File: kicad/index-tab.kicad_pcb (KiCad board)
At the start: 2 copper layers, 254 x 140.1 mm, 179 parts, among them J1 USB_C_Receptacle_USB2.0, SW1 SW_Push, U1 ATmega32U4-MU, U2 MIC5219-5.0YM5, Y1 16MHz

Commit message: Switched to 0603 and redrawn the PCB
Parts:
- removed C9: 100nF, Capacitor_SMD:C_1206_3216Metric_Pad1.42x1.75mm_HandSolder
- removed D101: PRTR5V0U2X, Package_TO_SOT_SMD:SOT-143
- removed D103: LED, LED_SMD:LED_1206_3216Metric_Pad1.42x1.75mm_HandSolder
- removed REF** (x2): Stabilizer_MX_2u, index-tab:Stabilizer_MX_2u
- removed U2: MIC5219-5.0YM5, Package_TO_SOT_SMD:SOT-23-5_HandSoldering
- added LED1: LED, LED_SMD:LED_0603_1608Metric_Pad1.05x0.95mm_HandSolder, B.Cu at (275.9, 44.8)
- C1, C2, C4: footprint Capacitor_SMD:C_1206_3216Metric_Pad1.42x1.75mm_HandSolder -> Capacitor_SMD:C_0603_1608Metric_Pad1.05x0.95mm_HandSolder
- C3: value 100nF -> 0.1uF; footprint Capacitor_SMD:C_1206_3216Metric_Pad1.42x1.75mm_HandSolder -> Capacitor_SMD:C_0603_1608Metric_Pad1.05x0.95mm_HandSolder
- C5: value 1uF -> 10uF; footprint Capacitor_SMD:C_1206_3216Metric_Pad1.42x1.75mm_HandSolder -> Capacitor_SMD:C_0603_1608Metric_Pad1.05x0.95mm_HandSolder
- C6, C7: value 10uF -> 1uF; footprint Capacitor_SMD:C_1206_3216Metric_Pad1.42x1.75mm_HandSolder -> Capacitor_SMD:C_0603_1608Metric_Pad1.05x0.95mm_HandSolder
- C8: value 1uF -> 0.1uF; footprint Capacitor_SMD:C_1206_3216Metric_Pad1.42x1.75mm_HandSolder -> Capacitor_SMD:C_0603_1608Metric_Pad1.05x0.95mm_HandSolder
- D1, D10, D11, D12, D13, D14, D15, D16, D17, D18, D19, D2, D20, D21, D22, D23, D24, D25, D26, D27, D28, D29, D3, D30, D31, D32, D33, D34, D35, D36, D37, D38, D39, D4, D40, D41, D42, D43, D44, D45, D46, D47, D48, D49, D5, D50, D51, D52, D53, D54, D55, D56, D57, D58, D59, D6, D60, D61, D62, D63, D64, D65, D66, D67, D68, D69, D7, D70, D71, D72, D73, D74, D75, D76, D8, D9: footprint Diode_SMD:D_1206_3216Metric_Pad1.42x1.75mm_HandSolder -> Diode_SMD:D_0603_1608Metric_Pad1.05x0.95mm_HandSolder
- D102: value D -> 3A/10V/280mV; footprint Diode_SMD:D_1206_3216Metric_Pad1.42x1.75mm_HandSolder -> Diode_SMD:D_SOD-323_HandSoldering
- F1: value 500mA -> 6v 0.5A
- R1, R2, R3, R4, R5, R6, R7: footprint Resistor_SMD:R_1206_3216Metric_Pad1.42x1.75mm_HandSolder -> Resistor_SMD:R_0603_1608Metric_Pad1.05x0.95mm_HandSolder
- U1: value ATmega32U4-MU -> ATmega32U4-AU; footprint Package_DFN_QFN:QFN-44-1EP_7x7mm_P0.5mm_EP5.2x5.2mm -> Package_QFP:TQFP-44_10x10mm_P0.8mm
- Y1: footprint Crystal:Crystal_SMD_3225-4Pin_3.2x2.5mm_HandSoldering -> Crystal:Crystal_SMD_0603-4Pin_6.0x3.5mm
- moved C7 53.6 mm to (270.6, 43.2)
- moved F1 42.8 mm to (268.0, 36.5), turned to 0 degrees
- moved D102 42.1 mm to (263.2, 36.5), turned to 0 degrees
- moved C6 40.4 mm to (254.9, 30.6), turned to 45 degrees
- moved C8 37.1 mm to (230.9, 34.0), turned to 180 degrees
- moved R5 33.1 mm to (257.3, 36.8), turned to 0 degrees
- moved C4 31.3 mm to (259.4, 30.8), turned to 0 degrees
- moved C2 17.9 mm to (256.9, 42.9), turned to 45 degrees
- moved C3 16.8 mm to (234.3, 27.0)
- moved C1 16.7 mm to (259.4, 40.4), turned to 45 degrees
- moved Y1 15.4 mm to (263.9, 44.0), turned to 180 degrees
- moved R4 13.4 mm to (251.4, 27.4), turned to 45 degrees
- moved C5 13.0 mm to (230.9, 31.0), turned to 180 degrees
- moved U1 9.24 mm to (245.6, 36.4), turned to 225 degrees
- moved R6 8.67 mm to (234.1, 38.2), turned to 0 degrees
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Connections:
- net Net-(C4-Pad1) renamed /UCAP
- net Net-(R5-Pad1) renamed /RESET
- C3 pad 1: GND -> /AREF
- C3 pad 2: Net-(C3-Pad2) -> GND
- C5 pad 1: /UVCC -> /+5v
- C6 pad 1: Net-(C6-Pad1) -> /V_USB
- C7 pad 1: /VCC -> /+5v
- C8 pad 1: /VCC -> /+5v
- D102 pad 1: Net-(C6-Pad1) -> /+5v
- F1 pad 1: /UVCC -> Net-(D102-Pad2)
- F1 pad 2: Net-(D102-Pad2) -> /V_USB
- J1 pad A4: /UVCC -> /V_USB
- J1 pad A6: Net-(D101-Pad2) -> /D+
- J1 pad A7: Net-(D101-Pad3) -> /D-
- J1 pad A9: /UVCC -> /V_USB
- J1 pad B4: /UVCC -> /V_USB
- J1 pad B6: Net-(D101-Pad2) -> /D+
- J1 pad B7: Net-(D101-Pad3) -> /D-
- J1 pad B9: /UVCC -> /V_USB
- J1 pad S1: GND -> Net-(J1-PadS1)
- R1 pad 1: Net-(J1-PadA5) -> GND
- R1 pad 2: GND -> Net-(J1-PadA5)
- R3 pad 2: Net-(D101-Pad3) -> /D+
- R4 pad 2: Net-(D101-Pad2) -> /D-
- R5 pad 2: /VCC -> /+5v
- R7 pad 1: /VCC -> Net-(LED1-Pad2)
- R7 pad 2: Net-(D103-Pad2) -> /+5v
- U1 pad 10: COL7 -> Net-(U1-Pad10)
- U1 pad 11: COL6 -> Net-(U1-Pad11)
- U1 pad 12: COL5 -> Net-(U1-Pad12)
- U1 pad 14: /VCC -> /+5v
- U1 pad 18: COL4 -> ROW5
- U1 pad 19: COL3 -> ROW4
- U1 pad 2: /UVCC -> /V_USB
- U1 pad 20: COL2 -> ROW3
- U1 pad 21: COL1 -> ROW2
- U1 pad 22: COL0 -> ROW1
- U1 pad 24: /VCC -> /+5v
- U1 pad 25: Net-(U1-Pad25) -> ROW0
- U1 pad 26: Net-(U1-Pad26) -> COL12
- U1 pad 27: ROW5 -> COL11
- U1 pad 28: ROW4 -> COL10
- U1 pad 29: ROW3 -> COL9
- U1 pad 3: Net-(R3-Pad1) -> Net-(R4-Pad1)
- U1 pad 30: ROW2 -> COL8
- U1 pad 31: ROW1 -> COL7
- U1 pad 32: ROW0 -> COL6
- U1 pad 34: /VCC -> /+5v
- U1 pad 36: Net-(U1-Pad36) -> COL5
- U1 pad 37: Net-(U1-Pad37) -> COL4
- U1 pad 38: Net-(U1-Pad38) -> COL3
- U1 pad 39: COL12 -> COL2
- U1 pad 4: Net-(R4-Pad1) -> Net-(R3-Pad1)
- U1 pad 40: COL11 -> COL1
- U1 pad 41: COL10 -> COL0
- U1 pad 42: Net-(C3-Pad2) -> /AREF
- U1 pad 44: /VCC -> /+5v
- U1 pad 7: /UVCC -> /V_USB
- U1 pad 8: COL9 -> Net-(U1-Pad8)
- U1 pad 9: COL8 -> Net-(U1-Pad9)
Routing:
- net /VCC: track 177.5 -> 0.00 mm, vias 3 -> 0
- net /UVCC: track 121.3 -> 0.00 mm, vias 2 -> 0
- net /+5v: track 0.00 -> 74.0 mm, vias 0 -> 2
- net GND: track 267.3 -> 198.5 mm
- net ROW0: track 300.9 -> 253.3 mm
- net /V_USB: track 0.00 -> 40.8 mm
- net /D-: track 0.00 -> 31.2 mm, vias 0 -> 2
- net /D+: track 0.00 -> 28.9 mm, vias 0 -> 2
- net Net-(R3-Pad1): track 32.5 -> 4.68 mm, vias 2 -> 0
- net Net-(D101-Pad3): track 27.6 -> 0.00 mm, vias 2 -> 0
- net Net-(R4-Pad1): track 30.5 -> 3.93 mm, vias 2 -> 0
- net /RESET: track 15.9 -> 41.9 mm, vias 0 -> 2
- net Net-(D101-Pad2): track 25.5 -> 0.00 mm
- net Net-(C6-Pad1): track 18.9 -> 0.00 mm
- net /XTAL1: track 32.0 -> 13.1 mm
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- removed copper zone on B.Cu, net GND

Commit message: Added rounded corners to the pcb
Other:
- board size 254 x 140.1 mm -> 254 x 140 mm
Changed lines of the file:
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@@
   (general
     (thickness 1.6)
-    (drawings 7)
+    (drawings 14)
     (tracks 1074)
     (zones 0)
@@
       (net 88 COL0))
   )
-  (gr_line (start 210.75 36) (end 210.75 44) (layer Edge.Cuts) (width 0.12))
-  (gr_line (start 210.75 36) (end 221.85 24.95) (layer Edge.Cuts) (width 0.12))
-  (gr_line (start 279 24.95) (end 221.85 24.95) (layer Edge.Cuts) (width 0.12))
-  (gr_line (start 25 44) (end 25 165) (layer Edge.Cuts) (width 0.12))
-  (gr_line (start 279 165) (end 279 24.95) (layer Edge.Cuts) (width 0.12))
-  (gr_line (start 25 165) (end 279 165) (layer Edge.Cuts) (width 0.12))
-  (gr_line (start 25 44) (end 210.75 44) (layer Edge.Cuts) (width 0.12))
+  (gr_arc (start 211.15 36) (end 210.9 35.7) (angle -50.21937124) (layer Edge.Cuts) (width 0.12))
+  (gr_arc (start 222 25.5) (end 222 25) (angle -48.81407483) (layer Edge.Cuts) (width 0.12))
+  (gr_arc (start 278.5 164.5) (end 278.5 165) (angle -90) (layer Edge.Cuts) (width 0.12))
+  (gr_arc (start 25.5 164.5) (end 25 164.5) (angle -90) (layer Edge.Cuts) (width 0.12))
+  (gr_arc (start 25.5 44.5) (end 25.5 44) (angle -90) (layer Edge.Cuts) (width 0.12))
+  (gr_arc (start 210.25 43.5) (end 210.25 44) (angle -90) (layer Edge.Cuts) (width 0.12))
+  (gr_arc (start 278 26) (end 279 26) (angle -90) (layer Edge.Cuts) (width 0.12))
+  (gr_line (start 210.759488 36.00017) (end 210.75 43.5) (layer Edge.Cuts) (width 0.12))
+  (gr_line (start 210.9 35.7) (end 221.623712 25.170748) (layer Edge.Cuts) (width 0.12))
+  (gr_line (start 278 25) (end 222 25) (layer Edge.Cuts) (width 0.12))
+  (gr_line (start 25 44.5) (end 25 164.5) (layer Edge.Cuts) (width 0.12))
+  (gr_line (start 279 164.5) (end 279 26) (layer Edge.Cuts) (width 0.12))
+  (gr_line (start 25.5 165) (end 278.5 165) (layer Edge.Cuts) (width 0.12))
+  (gr_line (start 25.5 44) (end 210.25 44) (layer Edge.Cuts) (width 0.12))
   (segment (start 264.112564 39.762564) (end 260.592685 39.762564) (width 0.25) (layer B.Cu) (net 1))
   (segment (start 260.592685 39.762564) (end 259.987436 39.762564) (width 0.25) (layer B.Cu) (net 1))

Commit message: Moved some components for better fillzone
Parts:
- moved C8 29.2 mm to (260.0, 35.6), turned to 90 degrees
- moved C5 26.6 mm to (257.3, 34.7)
- moved C7 12.9 mm to (261.9, 33.7), turned to 90 degrees
- moved C6 10.4 mm to (265.2, 30.1), turned to 0 degrees
- moved C4 6.42 mm to (265.2, 28.1)
- moved R4 2.57 mm to (253.9, 27.7), turned to 0 degrees
- moved R3 1.45 mm to (253.9, 29.4), turned to 0 degrees
- moved R1 0.81 mm to (275.7, 27.8)
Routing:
- net GND: track 198.5 -> 12.2 mm, vias 0 -> 13
- net /+5v: track 74.0 -> 80.4 mm, vias 2 -> 4
- net /UCAP: track 10.0 -> 16.5 mm
- net /D-: track 31.2 -> 27.2 mm
- net /D+: track 28.9 -> 25.6 mm
- net Net-(R4-Pad1): track 3.93 -> 6.32 mm
- net Net-(R3-Pad1): track 4.68 -> 6.31 mm
- net (no net): track 0.00 -> 1.51 mm
- net /V_USB: track 40.8 -> 39.6 mm
- net Net-(J1-PadA5): track 7.89 -> 7.05 mm
- added copper zone on B.Cu, net GND
- added copper zone on F.Cu, net GND
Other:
- net class Power added: clearance 0.2, trace_width 0.381, via_dia 0.8, via_drill 0.4

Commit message: Added RGB and a monster to the f.silk
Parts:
- added CR1: 0.1uF, Capacitor_SMD:C_0603_1608Metric_Pad1.05x0.95mm_HandSolder, B.Cu at (256.6, 65.0)
- added CR10: 0.1uF, Capacitor_SMD:C_0603_1608Metric_Pad1.05x0.95mm_HandSolder, B.Cu at (257.8, 106.8)
- added CR2: 0.1uF, Capacitor_SMD:C_0603_1608Metric_Pad1.05x0.95mm_HandSolder, B.Cu at (197.6, 65.2)
- added CR3: 0.1uF, Capacitor_SMD:C_0603_1608Metric_Pad1.05x0.95mm_HandSolder, B.Cu at (124.0, 69.3)
- added CR4: 0.1uF, Capacitor_SMD:C_0603_1608Metric_Pad1.05x0.95mm_HandSolder, B.Cu at (48.0, 69.5)
- added CR5: 0.1uF, Capacitor_SMD:C_0603_1608Metric_Pad1.05x0.95mm_HandSolder, B.Cu at (47.9, 106.5)
- added CR6: 0.1uF, Capacitor_SMD:C_0603_1608Metric_Pad1.05x0.95mm_HandSolder, B.Cu at (30.2, 143.1)
- added CR7: 0.1uF, Capacitor_SMD:C_0603_1608Metric_Pad1.05x0.95mm_HandSolder, B.Cu at (109.0, 146.0)
- added CR8: 0.1uF, Capacitor_SMD:C_0603_1608Metric_Pad1.05x0.95mm_HandSolder, B.Cu at (208.6, 142.9)
- added CR9: 0.1uF, Capacitor_SMD:C_0603_1608Metric_Pad1.05x0.95mm_HandSolder, B.Cu at (258.3, 143.7)
- added G***: LOGO, index-tab:monster, F.Cu at (219.0, 110.2)
- added RGB1: WS2812B, LED_SMD:LED_WS2812B_PLCC4_5.0x5.0mm_P3.2mm, B.Cu at (266.8, 64.1)
- added RGB10: WS2812B, LED_SMD:LED_WS2812B_PLCC4_5.0x5.0mm_P3.2mm, B.Cu at (266.6, 104.1)
- added RGB2: WS2812B, LED_SMD:LED_WS2812B_PLCC4_5.0x5.0mm_P3.2mm, B.Cu at (190.3, 65.8)
- added RGB3: WS2812B, LED_SMD:LED_WS2812B_PLCC4_5.0x5.0mm_P3.2mm, B.Cu at (114.7, 65.8)
- added RGB4: WS2812B, LED_SMD:LED_WS2812B_PLCC4_5.0x5.0mm_P3.2mm, B.Cu at (37.9, 65.8)
- added RGB5: WS2812B, LED_SMD:LED_WS2812B_PLCC4_5.0x5.0mm_P3.2mm, B.Cu at (38.2, 103.9)
- added RGB6: WS2812B, LED_SMD:LED_WS2812B_PLCC4_5.0x5.0mm_P3.2mm, B.Cu at (37.5, 142.1)
- added RGB7: WS2812B, LED_SMD:LED_WS2812B_PLCC4_5.0x5.0mm_P3.2mm, B.Cu at (108.8, 151.6)
- added RGB8: WS2812B, LED_SMD:LED_WS2812B_PLCC4_5.0x5.0mm_P3.2mm, B.Cu at (194.8, 153.2)
- added RGB9: WS2812B, LED_SMD:LED_WS2812B_PLCC4_5.0x5.0mm_P3.2mm, B.Cu at (266.4, 142.1)
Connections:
- J1 pad S1: Net-(J1-PadS1) -> GND
- U1 pad 1: Net-(U1-Pad1) -> RGB
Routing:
- net /+5v: track 80.4 -> 881.7 mm, vias 4 -> 8
- net Net-(RGB7-Pad2): track 0.00 -> 89.3 mm
- net Net-(RGB1-Pad2): track 0.00 -> 79.2 mm
- net Net-(RGB8-Pad2): track 0.00 -> 76.4 mm
- net Net-(RGB3-Pad2): track 0.00 -> 73.7 mm
- net Net-(RGB2-Pad2): track 0.00 -> 72.5 mm
- net Net-(RGB6-Pad2): track 0.00 -> 69.6 mm
- net RGB: track 0.00 -> 65.1 mm
- net Net-(RGB5-Pad2): track 0.00 -> 51.1 mm
- net Net-(RGB4-Pad2): track 0.00 -> 50.0 mm
- net Net-(RGB10-Pad4): track 0.00 -> 45.4 mm, vias 0 -> 2
- net (no net): track 1.51 -> 0.00 mm
- net ROW4: track 367.7 -> 367.2 mm
- net GND: vias 13 -> 37

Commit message: Moved diode and rgb footprint
Need to create new traces too, but later
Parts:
- removed G***: LOGO, index-tab:monster
- D1, D10, D11, D12, D13, D14, D15, D16, D17, D18, D19, D2, D20, D21, D22, D23, D24, D25, D26, D27, D28, D29, D3, D30, D31, D32, D33, D34, D35, D36, D37, D38, D39, D4, D40, D41, D42, D43, D44, D45, D46, D47, D48, D49, D5, D50, D51, D52, D53, D54, D55, D56, D57, D58, D59, D6, D60, D61, D62, D63, D64, D65, D66, D67, D68, D69, D7, D70, D71, D72, D73, D74, D75, D76, D8, D9: footprint Diode_SMD:D_0603_1608Metric_Pad1.05x0.95mm_HandSolder -> Diode_SMD:D_SOD-123
- moved CR4 20.7 mm to (27.8, 65.0)
- moved CR5 20.3 mm to (27.8, 103.9)
- moved CR1 19.7 mm to (276.2, 65.8)
- moved CR3 19.6 mm to (104.8, 65.8)
- moved CR9 18.8 mm to (277.0, 142.0)
- moved CR10 17.9 mm to (275.4, 103.9)
- moved CR2 16.7 mm to (181.0, 67.4)
- moved CR8 16.6 mm to (194.5, 151.5)
- moved D5 14.1 mm to (44.6, 138.6)
- moved D3 14.1 mm to (44.6, 100.5)
- moved D1 14.1 mm to (44.6, 62.4)
- moved D25 14.1 mm to (120.8, 62.4)
- moved D47 14.0 mm to (197.0, 62.4)
- moved RGB3 10.7 mm to (104.8, 61.9)
- moved RGB2 10.1 mm to (181.0, 61.9)
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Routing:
- net ROW0: track 253.3 -> 24.6 mm
- net Net-(RGB1-Pad2): track 79.2 -> 307.9 mm
- net Net-(RGB3-Pad2): track 73.7 -> 0.00 mm
- net COL4: track 240.2 -> 313.9 mm, vias 7 -> 8
- net Net-(RGB10-Pad4): track 45.4 -> 0.00 mm, vias 2 -> 0
- net GND: track 12.2 -> 57.5 mm
- net COL8: vias 7 -> 8

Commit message: Retraced and rebuild the PCB
Fixed wrong footprint for diodes and crystal. Trying out a new USB-C, but probably changing back before order of rev2. Also added ESD for safty.
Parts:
- removed C8: 0.1uF, Capacitor_SMD:C_0603_1608Metric_Pad1.05x0.95mm_HandSolder
- removed D102: 3A/10V/280mV, Diode_SMD:D_SOD-323_HandSoldering
- removed LED1: LED, LED_SMD:LED_0603_1608Metric_Pad1.05x0.95mm_HandSolder
- removed R7: 1K, Resistor_SMD:R_0603_1608Metric_Pad1.05x0.95mm_HandSolder
- added D101: PRTR5V0U2X, Package_TO_SOT_SMD:SOT-143, B.Cu at (268.2, 34.5)
- C1, C2: value 22p -> 22pF
- C3: value 0.1uF -> 1uF
- C5: value 10uF -> 0.1uF
- C7: value 1uF -> 0.1uF
- J1: footprint Connector_USB:USB_C_Receptacle_HRO_TYPE-C-31-M-12 -> Connector_USB:USB_C_Receptacle_GCT_USB4085
- Y1: footprint Crystal:Crystal_SMD_0603-4Pin_6.0x3.5mm -> Crystal:Crystal_SMD_3225-4Pin_3.2x2.5mm_HandSoldering
- moved C3 36.0 mm to (270.2, 29.6), turned to 90 degrees
- moved R5 21.7 mm to (237.0, 29.0)
- moved CR4 20.4 mm to (47.8, 69.0)
- moved CR9 19.8 mm to (257.3, 143.0)
- moved CR1 18.8 mm to (257.6, 67.9), turned to 270 degrees
- moved Y1 16.2 mm to (247.8, 45.6)
- moved C2 14.8 mm to (242.1, 44.5), turned to 0 degrees
- moved R1 13.9 mm to (265.9, 37.6), turned to 0 degrees
- moved C7 13.3 mm to (250.7, 26.6), turned to 0 degrees
- moved CR6 12.9 mm to (39.9, 140.6), turned to 90 degrees
- moved R2 12.5 mm to (274.8, 29.2), turned to 180 degrees
- moved CR5 11.4 mm to (38.9, 101.6), turned to 90 degrees
- moved CR10 10.6 mm to (264.9, 104.3), turned to 90 degrees
- moved C6 10.1 mm to (257.3, 36.2), turned to 315 degrees
- moved C5 9.36 mm to (265.1, 29.6), turned to 270 degrees
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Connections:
- C3 pad 1: /AREF -> /V_BUS
- C4 pad 1: /UCAP -> /+5v
- C6 pad 1: /V_USB -> /UCAP
- C7 pad 1: /+5v -> /AREF
- F1 pad 1: Net-(D102-Pad2) -> /+5v
- F1 pad 2: /V_USB -> /V_BUS
- J1 pad A4: /V_USB -> /V_BUS
- J1 pad A9: /V_USB -> /V_BUS
- J1 pad B4: /V_USB -> /V_BUS
- J1 pad B9: /V_USB -> /V_BUS
- U1 pad 10: Net-(U1-Pad10) -> ROW3
- U1 pad 11: Net-(U1-Pad11) -> ROW2
- U1 pad 12: Net-(U1-Pad12) -> ROW1
- U1 pad 18: ROW5 -> COL12
- U1 pad 19: ROW4 -> COL11
- U1 pad 2: /V_USB -> /V_BUS
- U1 pad 20: ROW3 -> COL10
- U1 pad 21: ROW2 -> COL9
- U1 pad 22: ROW1 -> COL8
- U1 pad 26: COL12 -> COL7
- U1 pad 27: COL11 -> COL6
- U1 pad 28: COL10 -> COL5
- U1 pad 29: COL9 -> COL4
- U1 pad 30: COL8 -> COL3
- U1 pad 31: COL7 -> COL2
- U1 pad 32: COL6 -> COL1
- U1 pad 36: COL5 -> COL0
- U1 pad 37: COL4 -> Net-(U1-Pad37)
- U1 pad 38: COL3 -> Net-(U1-Pad38)
- U1 pad 39: COL2 -> Net-(U1-Pad39)
- U1 pad 40: COL1 -> Net-(U1-Pad40)
- U1 pad 41: COL0 -> Net-(U1-Pad41)
- U1 pad 7: /V_USB -> /V_BUS
- U1 pad 8: Net-(U1-Pad8) -> ROW5
- U1 pad 9: Net-(U1-Pad9) -> ROW4
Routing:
- net ROW0: track 24.6 -> 263.6 mm
- net Net-(RGB1-Pad2): track 307.9 -> 86.5 mm
- net COL4: track 313.9 -> 238.0 mm, vias 8 -> 7
- net Net-(RGB3-Pad2): track 0.00 -> 70.3 mm
- net /V_BUS: track 0.00 -> 57.1 mm
- net Net-(RGB10-Pad4): track 0.00 -> 43.1 mm, vias 0 -> 2
- net /V_USB: track 39.6 -> 0.00 mm
- net ROW1: track 309.8 -> 344.2 mm
- net /+5v: track 881.7 -> 913.2 mm, vias 8 -> 4
- net GND: track 57.5 -> 26.1 mm, vias 37 -> 9
- net ROW2: track 327.8 -> 307.7 mm
- net ROW4: track 367.2 -> 347.8 mm
- net COL11: track 139.7 -> 126.3 mm
- net Net-(RGB7-Pad2): track 89.3 -> 102.4 mm
- net COL12: track 157.3 -> 144.4 mm
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
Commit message: Changed USB-C and added more gnd
Suing the easier HRO TYPE-C-31-M-12
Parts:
- added G***: LOGO, index-tab:monster, F.Cu at (219.8, 109.9)
- J1: footprint Connector_USB:USB_C_Receptacle_GCT_USB4085 -> Connector_USB:USB_C_Receptacle_HRO_TYPE-C-31-M-12
- moved R1 13.2 mm to (274.8, 42.4)
- moved R2 12.5 mm to (274.8, 28.9)
- moved J1 4.45 mm to (276.9, 35.5)
- renumbered R2 to R1, R1 to R2
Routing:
- net /V_BUS: track 57.1 -> 54.0 mm
- net GND: track 26.1 -> 23.0 mm, vias 9 -> 38
- net Net-(J1-PadA5): track 6.18 -> 7.79 mm
- net /D+: track 14.5 -> 16.0 mm
- net Net-(J1-PadB5): track 6.93 -> 7.60 mm
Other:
- board text added: "Index Tab"
- board text added: "by kyrremann.no | rev2"

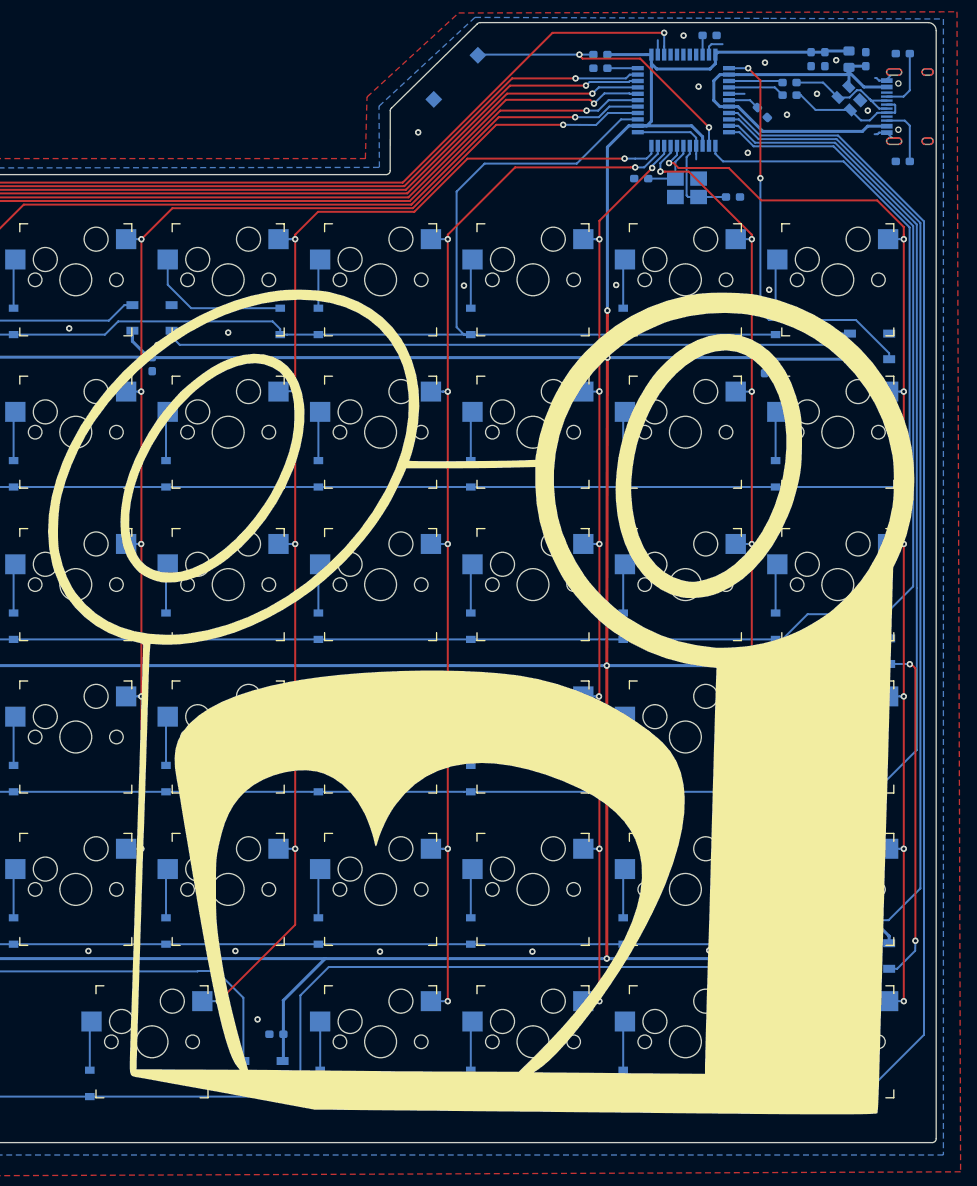
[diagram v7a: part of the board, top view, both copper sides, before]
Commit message: rev2 ordered
this was done before I've managed to get rev1 working. Post coming about it. rev2 looks more like UT47.2
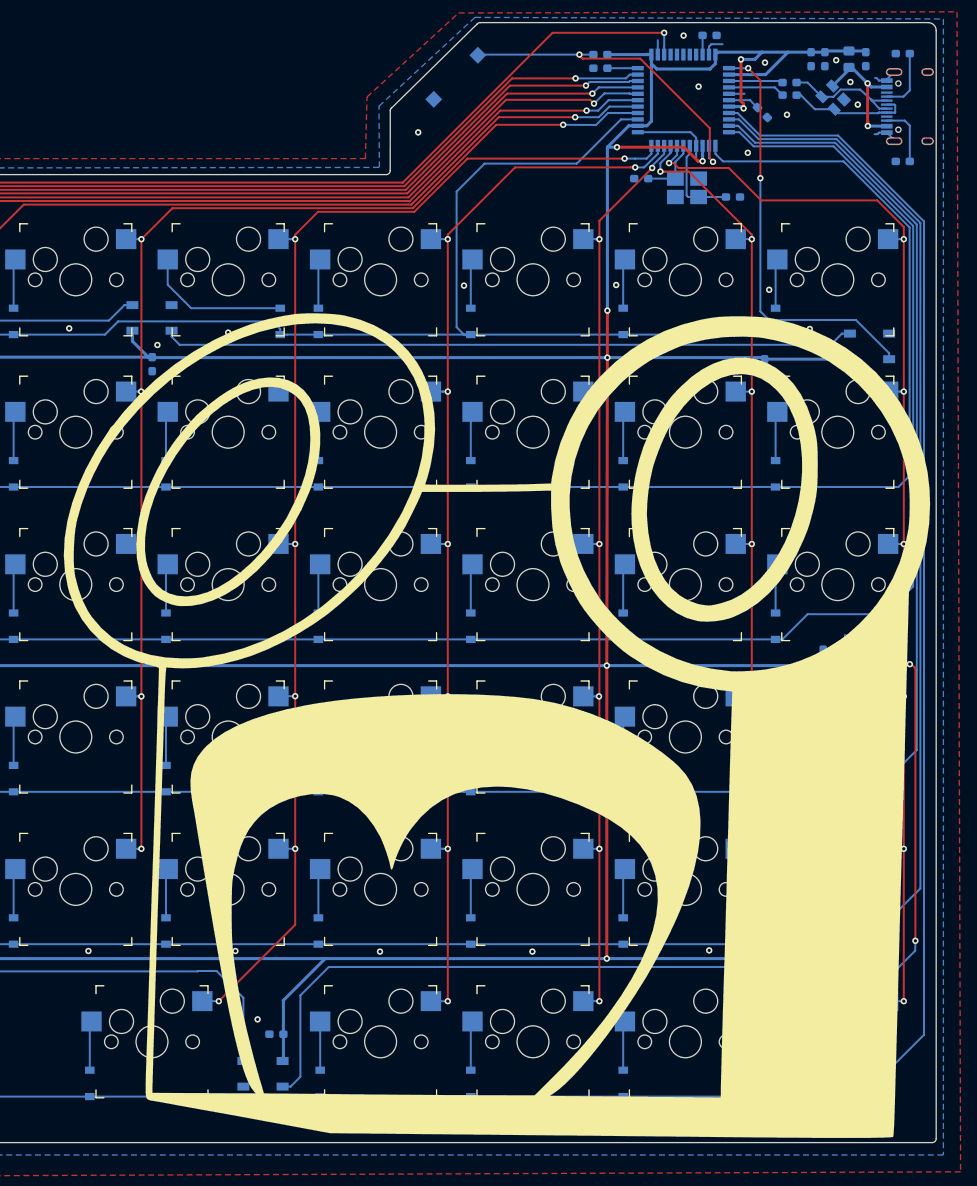
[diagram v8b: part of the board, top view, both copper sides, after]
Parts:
- moved G*** 3.55 mm to (221.7, 112.9)
- moved D101 2.03 mm to (266.1, 34.4)
- turned C3 to 270 degrees
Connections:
- C3 pad 1: /V_BUS -> /+5v
- U1 pad 2: /V_BUS -> /+5v
- U1 pad 7: /V_BUS -> /+5v
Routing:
- net /V_BUS: track 54.0 -> 16.7 mm, vias 0 -> 2
- net /+5v: track 913.2 -> 940.0 mm, vias 4 -> 8
- net /RESET: track 36.8 -> 41.3 mm
- net /D+: track 16.0 -> 15.3 mm
